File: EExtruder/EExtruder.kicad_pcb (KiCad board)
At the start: 2 copper layers, 73.4 x 47.1 mm, 97 parts, among them J1 20A 50V, J11 Conn_01x03_Male, J2 AudioJack4, J3 6A 50V, J4 6A 50V, J5 Conn_01x02, J6 Conn_01x02, J7 Conn_01x03_Male, J8 Conn_01x03_Male, J9 Conn_01x03_Male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

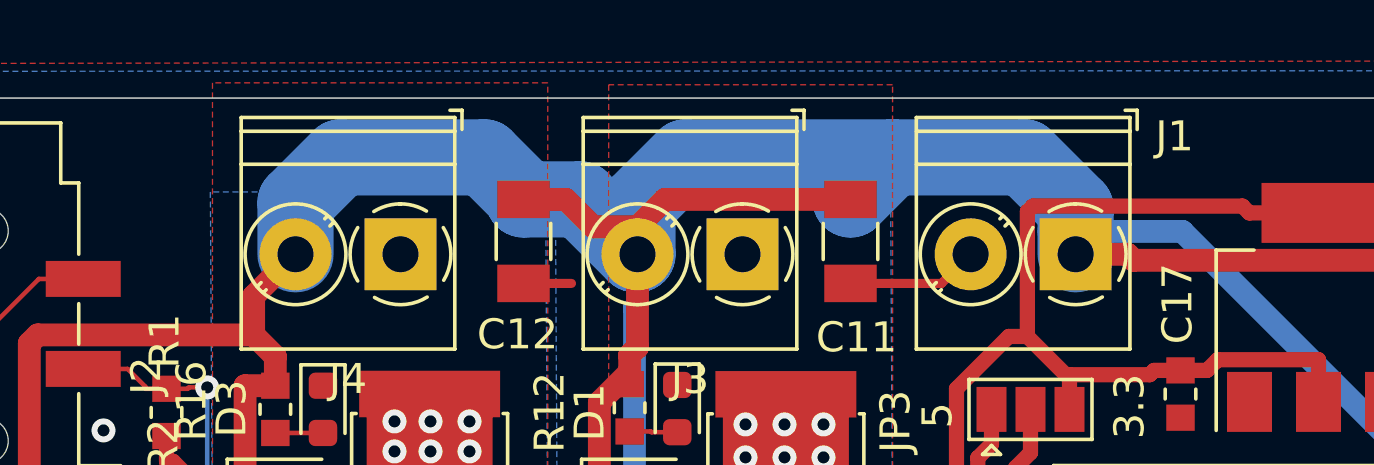
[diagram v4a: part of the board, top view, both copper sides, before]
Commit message: Added more labels and sent to FAB.
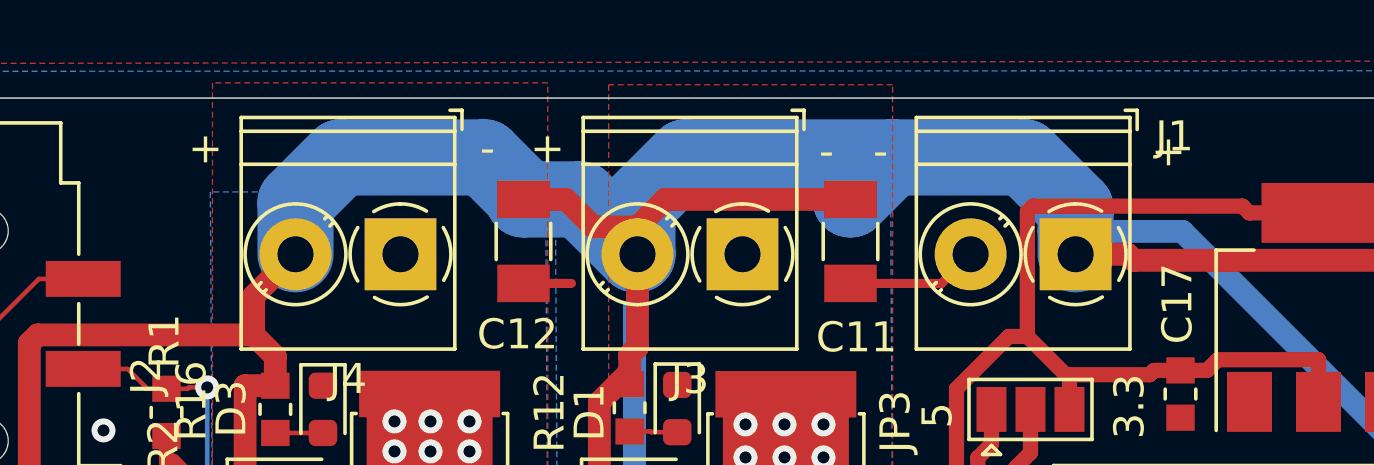
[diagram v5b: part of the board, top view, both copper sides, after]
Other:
- board text added: "+"
- board text added: "-"
- board text added: "PWR"
- board text added: "RX"
- board text added: "TX"
- board text added: "~CS"
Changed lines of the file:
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@@
   (general
     (thickness 1.6)
-    (drawings 44)
+    (drawings 59)
     (tracks 1095)
     (zones 0)
@@
     )
   )
+  (gr_text - (at 162.2 84.9) (layer F.SilkS)
+    (effects (font (size 1 1) (thickness 0.15)))
+  )
+  (gr_text + (at 141.5 84.8) (layer F.SilkS)
+    (effects (font (size 1 1) (thickness 0.15)))
+  )
+  (gr_text - (at 150.9 84.8) (layer F.SilkS)
+    (effects (font (size 1 1) (thickness 0.15)))
+  )
+  (gr_text + (at 152.9 84.8) (layer F.SilkS)
+    (effects (font (size 1 1) (thickness 0.15)))
+  )
+  (gr_text - (at 164 84.9) (layer F.SilkS)
+    (effects (font (size 1 1) (thickness 0.15)))
+  )
+  (gr_text + (at 173.6 84.9) (layer F.SilkS)
+    (effects (font (size 1 1) (thickness 0.15)))
+  )
+  (gr_text GND (at 190.1 125.7) (layer B.SilkS)
+    (effects (font (size 1 1) (thickness 0.15)) (justify mirror))
+  )
+  (gr_text TX (at 184.8 125.7) (layer B.SilkS)
+    (effects (font (size 1 1) (thickness 0.15)) (justify mirror))
+  )
+  (gr_text RX (at 187.4 125.7) (layer B.SilkS)
+    (effects (font (size 1 1) (thickness 0.15)) (justify mirror))
+  )
+  (gr_text PWR (at 168.6 93.7 90) (layer B.SilkS)
+    (effects (font (size 1 1) (thickness 0.15)) (justify mirror))
+  )
+  (gr_text GND (at 171.1 93.8 90) (layer B.SilkS)
+    (effects (font (size 1 1) (thickness 0.15)) (justify mirror))
+  )
+  (gr_text MISO (at 173.7 93.5 90) (layer B.SilkS)
+    (effects (font (size 1 1) (thickness 0.15)) (justify mirror))
+  )
+  (gr_text MOSI (at 176.3 93.4 90) (layer B.SilkS)
+    (effects (font (size 1 1) (thickness 0.15)) (justify mirror))
+  )
+  (gr_text SCK (at 178.8 93.8 90) (layer B.SilkS)
+    (effects (font (size 1 1) (thickness 0.15)) (justify mirror))
+  )
+  (gr_text ~CS (at 181.4 94.1 90) (layer B.SilkS)
+    (effects (font (size 1 1) (thickness 0.15)) (justify mirror))
+  )
   (gr_text 3.3 (at 174.9 108.3) (layer F.SilkS)
     (effects (font (size 1 1) (thickness 0.15)))
@@
   (gr_line (start 201.4 83.1215) (end 201.4 130.175) (layer Edge.Cuts) (width 0.05))
   (gr_line (start 127.9525 83.1215) (end 201.4 83.1215) (layer Edge.Cuts) (width 0.05))
-  (via (at 149 94.9) (size 0.8) (drill 0.4) (layers F.Cu B.Cu) (net 13))
-  (via (at 147.8 94.9) (size 0.8) (drill 0.4) (layers F.Cu B.Cu) (net 13))
-  (via (at 147.8 96) (size 0.8) (drill 0.4) (layers F.Cu B.Cu) (net 13))
-  (via (at 149 96) (size 0.8) (drill 0.4) (layers F.Cu B.Cu) (net 13))
-  (via (at 150.3 96) (size 0.8) (drill 0.4) (layers F.Cu B.Cu) (net 13))
-  (via (at 150.3 94.9) (size 0.8) (drill 0.4) (layers F.Cu B.Cu) (net 13))
-  (via (at 150.3 93.9) (size 0.8) (drill 0.4) (layers F.Cu B.Cu) (net 13))
-  (via (at 149 93.9) (size 0.8) (drill 0.4) (layers F.Cu B.Cu) (net 13))
-  (via (at 147.8 93.9) (size 0.8) (drill 0.4) (layers F.Cu B.Cu) (net 13))
-  (via (at 160.8 96.2) (size 0.8) (drill 0.4) (layers F.Cu B.Cu) (net 11))
-  (via (at 159.5 96.2) (size 0.8) (drill 0.4) (layers F.Cu B.Cu) (net 11))
-  (via (at 159.5 95.1) (size 0.8) (drill 0.4) (layers F.Cu B.Cu) (net 11))
-  (via (at 160.8 95.1) (size 0.8) (drill 0.4) (layers F.Cu B.Cu) (net 11))
-  (via (at 162.1 96.2) (size 0.8) (drill 0.4) (layers F.Cu B.Cu) (net 11))
-  (via (at 162.1 95.1) (size 0.8) (drill 0.4) (layers F.Cu B.Cu) (net 11))
-  (via (at 162.1 94) (size 0.8) (drill 0.4) (layers F.Cu B.Cu) (net 11))
-  (via (at 160.8 94) (size 0.8) (drill 0.4) (layers F.Cu B.Cu) (net 11))
-  (via (at 159.5 94) (size 0.8) (drill 0.4) (layers F.Cu B.Cu) (net 11))
   (segment (start 153.3182 113.526) (end 152.704545 114.139655) (width 0.3048) (layer F.Cu) (net 1))
   (segment (start 154.273 113.526) (end 153.3182 113.526) (width 0.3048) (layer F.Cu) (net 1))
@@
   (segment (start 157.226 94.2595) (end 156.3674 94.2595) (width 0.1524) (layer F.Cu) (net 10))
   (segment (start 156.3674 94.2595) (end 156.3419 94.234) (width 0.1524) (layer F.Cu) (net 10))
+  (via (at 160.8 96.2) (size 0.8) (drill 0.4) (layers F.Cu B.Cu) (net 11))
+  (via (at 159.5 96.2) (size 0.8) (drill 0.4) (layers F.Cu B.Cu) (net 11))
+  (via (at 159.5 95.1) (size 0.8) (drill 0.4) (layers F.Cu B.Cu) (net 11))
+  (via (at 160.8 95.1) (size 0.8) (drill 0.4) (layers F.Cu B.Cu) (net 11))
+  (via (at 162.1 96.2) (size 0.8) (drill 0.4) (layers F.Cu B.Cu) (net 11))
+  (via (at 162.1 95.1) (size 0.8) (drill 0.4) (layers F.Cu B.Cu) (net 11))
+  (via (at 162.1 94) (size 0.8) (drill 0.4) (layers F.Cu B.Cu) (net 11))
+  (via (at 160.8 94) (size 0.8) (drill 0.4) (layers F.Cu B.Cu) (net 11))
+  (via (at 159.5 94) (size 0.8) (drill 0.4) (layers F.Cu B.Cu) (net 11))
   (segment (start 145.415 94.285) (end 143.828 94.285) (width 0.1524) (layer F.Cu) (net 12))
+  (via (at 149 94.9) (size 0.8) (drill 0.4) (layers F.Cu B.Cu) (net 13))
+  (via (at 147.8 94.9) (size 0.8) (drill 0.4) (layers F.Cu B.Cu) (net 13))
+  (via (at 147.8 96) (size 0.8) (drill 0.4) (layers F.Cu B.Cu) (net 13))
+  (via (at 149 96) (size 0.8) (drill 0.4) (layers F.Cu B.Cu) (net 13))
+  (via (at 150.3 96) (size 0.8) (drill 0.4) (layers F.Cu B.Cu) (net 13))
+  (via (at 150.3 94.9) (size 0.8) (drill 0.4) (layers F.Cu B.Cu) (net 13))
+  (via (at 150.3 93.9) (size 0.8) (drill 0.4) (layers F.Cu B.Cu) (net 13))
+  (via (at 149 93.9) (size 0.8) (drill 0.4) (layers F.Cu B.Cu) (net 13))
+  (via (at 147.8 93.9) (size 0.8) (drill 0.4) (layers F.Cu B.Cu) (net 13))
   (segment (start 154.273 114.526) (end 155.1519 114.526) (width 0.1524) (layer F.Cu) (net 14))
   (segment (start 156.254 113.7571) (end 155.9208 113.7571) (width 0.1524) (layer F.Cu) (net 14))

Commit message: Update to rev3.
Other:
- board text added: "EExtruder rev3"
- board text removed: "EExtruder rev2"
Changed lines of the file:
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@@
     (effects (font (size 1.5 1.5) (thickness 0.3)) (justify mirror))
   )
-  (gr_text "EExtruder\nrev2" (at 192.1 92.9) (layer B.SilkS)
+  (gr_text "EExtruder\nrev3" (at 192.1 92.9) (layer B.SilkS)
     (effects (font (size 1.5 1.5) (thickness 0.3)) (justify mirror))
   )

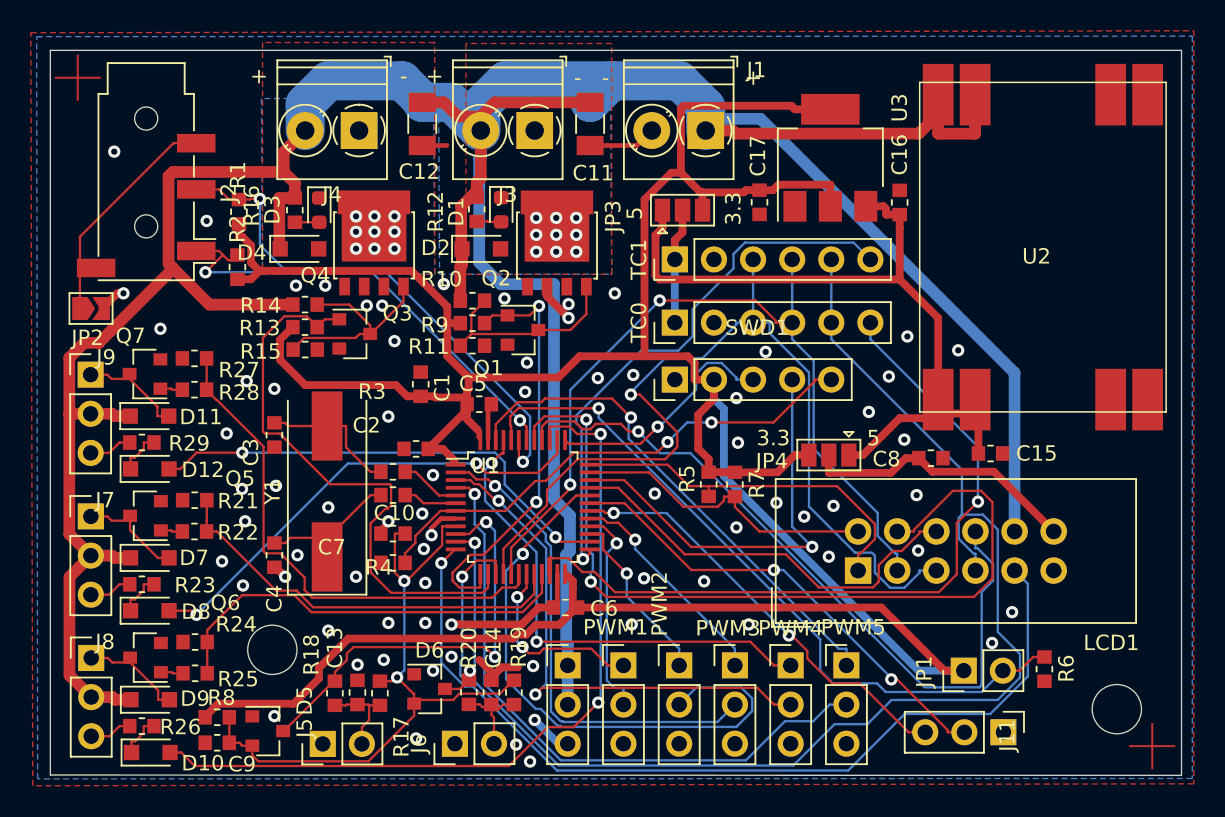
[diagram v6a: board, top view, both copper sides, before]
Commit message: Update ground plane. Power to MOSFETS. Heatpads for MOSFETS.
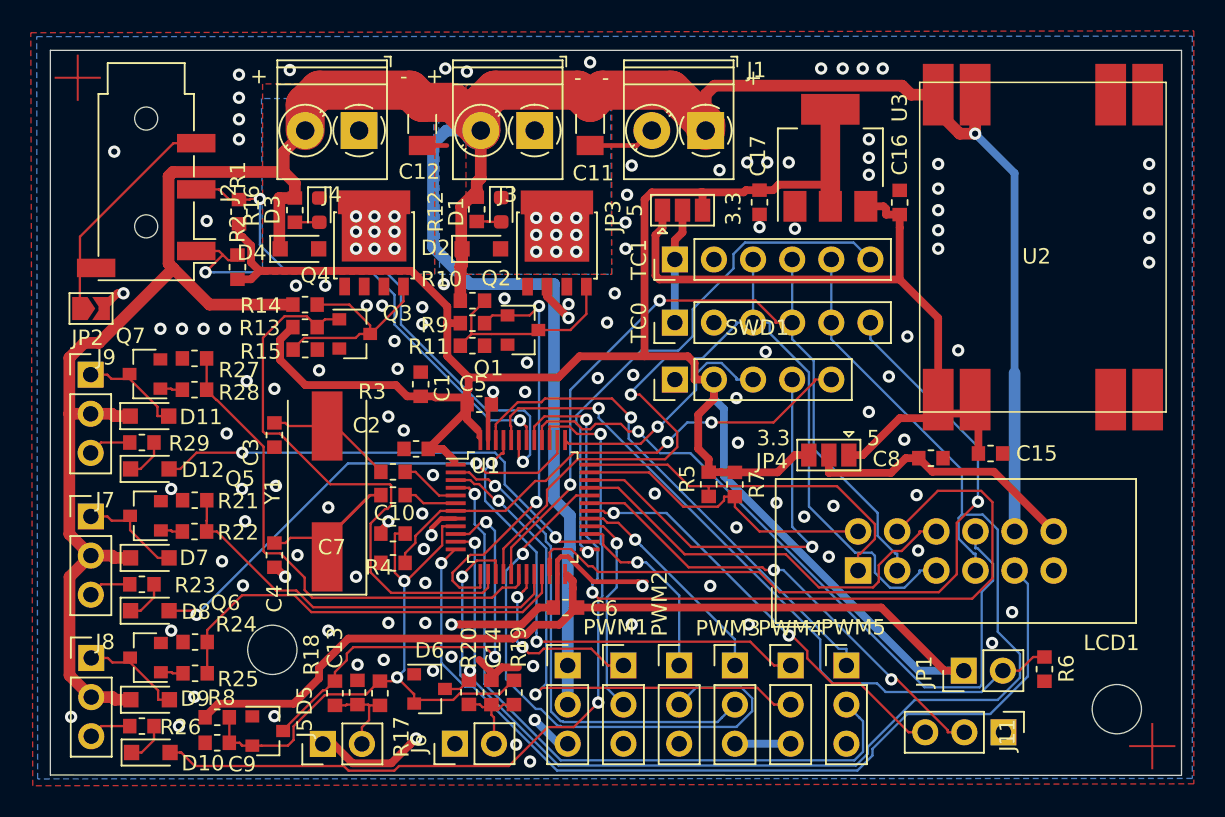
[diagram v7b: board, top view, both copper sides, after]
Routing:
- net /VIN: track 238.0 -> 219.3 mm, vias 0 -> 1
- net GND: track 33.0 -> 51.4 mm, vias 73 -> 123
- net /3.3V: track 206.7 -> 198.1 mm
- net Net-(C4-Pad1): track 9.44 -> 15.3 mm
- net /TACH5: track 41.1 -> 44.4 mm
- net /AVREF: track 43.1 -> 40.3 mm
- net /~TC0_CS: track 49.5 -> 51.2 mm
- net /SDA: track 34.3 -> 35.7 mm
- net /SCL: track 30.7 -> 31.9 mm
- net /~TC1_CS: track 36.1 -> 35.2 mm
- net /PWM2: track 11.5 -> 12.4 mm
- net Net-(C3-Pad1): track 9.04 -> 8.25 mm
- net /LCD_LED: track 55.0 -> 55.5 mm

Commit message: Added a few more vias.
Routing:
- net GND: vias 123 -> 131
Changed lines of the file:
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@@
     (thickness 1.6)
     (drawings 59)
-    (tracks 1172)
+    (tracks 1179)
     (zones 0)
     (modules 97)
@@
   )
   (setup
-    (last_trace_width 1.27)
+    (last_trace_width 0.762)
     (user_trace_width 0.1524)
     (user_trace_width 0.3048)
@@
   (via (at 176.3 94.7) (size 0.8) (drill 0.4) (layers F.Cu B.Cu) (net 1))
   (via (at 174 94.6) (size 0.8) (drill 0.4) (layers F.Cu B.Cu) (net 1))
+  (via (at 170.2 84.6) (size 0.8) (drill 0.4) (layers F.Cu B.Cu) (net 1))
+  (via (at 172.5 84) (size 0.8) (drill 0.4) (layers F.Cu B.Cu) (net 1))
+  (via (at 186.8 121.8) (size 0.8) (drill 0.4) (layers F.Cu B.Cu) (net 1))
+  (via (at 186.8 120.7) (size 0.8) (drill 0.4) (layers F.Cu B.Cu) (net 1))
+  (via (at 186.8 119.6) (size 0.8) (drill 0.4) (layers F.Cu B.Cu) (net 1))
+  (via (at 196.8 118.6) (size 0.8) (drill 0.4) (layers F.Cu B.Cu) (net 1))
+  (via (at 196.8 116.9) (size 0.8) (drill 0.4) (layers F.Cu B.Cu) (net 1))
+  (via (at 196.8 115.1) (size 0.8) (drill 0.4) (layers F.Cu B.Cu) (net 1))
   (segment (start 155.0125 105.8795) (end 155.0125 106.1) (width 0.508) (layer F.Cu) (net 2))
   (segment (start 155.0125 105.8795) (end 155.0125 105.6591) (width 0.508) (layer F.Cu) (net 2))
@@
   (segment (start 143.1054 91.0162) (end 143.1054 89.7231) (width 0.762) (layer F.Cu) (net 7))
   (segment (start 143.1054 89.7231) (end 144.5 88.3285) (width 0.762) (layer F.Cu) (net 7))
-  (segment (start 190.56 104.064) (end 190.56 114.36) (width 0.762) (layer B.Cu) (net 7))
   (segment (start 161.544 125.603) (end 161.544 123.063) (width 0.762) (layer B.Cu) (net 7))
   (segment (start 155.9 87.4142) (end 155.9 88.3285) (width 0.762) (layer F.Cu) (net 7))
@@
   (segment (start 155.9 88.3285) (end 155.828 88.3285) (width 2.54) (layer B.Cu) (net 7))
   (via (at 188 88.5337) (size 0.8) (drill 0.4) (layers F.Cu B.Cu) (net 7))
-  (segment (start 190.56 104.064) (end 190.56 91.0937) (width 0.508) (layer B.Cu) (net 7))
-  (segment (start 190.56 91.0937) (end 188 88.5337) (width 0.508) (layer B.Cu) (net 7))
   (segment (start 168.263753 85.706099) (end 163.793901 85.706099) (width 2.54) (layer F.Cu) (net 7))
   (segment (start 163.793901 85.706099) (end 163 86.5) (width 2.54) (layer F.Cu) (net 7))
@@
   (segment (start 170.505 85.995) (end 170.505 88.3285) (width 0.762) (layer F.Cu) (net 7))
   (segment (start 171.083401 85.416599) (end 170.505 85.995) (width 0.762) (layer F.Cu) (net 7))
+  (segment (start 190.56 91.0937) (end 188 88.5337) (width 0.762) (layer B.Cu) (net 7))
+  (segment (start 190.56 114.36) (end 190.56 91.0937) (width 0.762) (layer B.Cu) (net 7))
   (segment (start 148.182 128.156) (end 148.182 127.0771) (width 0.1524) (layer F.Cu) (net 8))
   (segment (start 148.182 127.0771) (end 148.6481 126.611) (width 0.1524) (layer F.Cu) (net 8))
